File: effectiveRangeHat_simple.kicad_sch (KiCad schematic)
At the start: 11 parts, among them J1 Raspberry_Pi_2_3, P1 USB4105GFA120

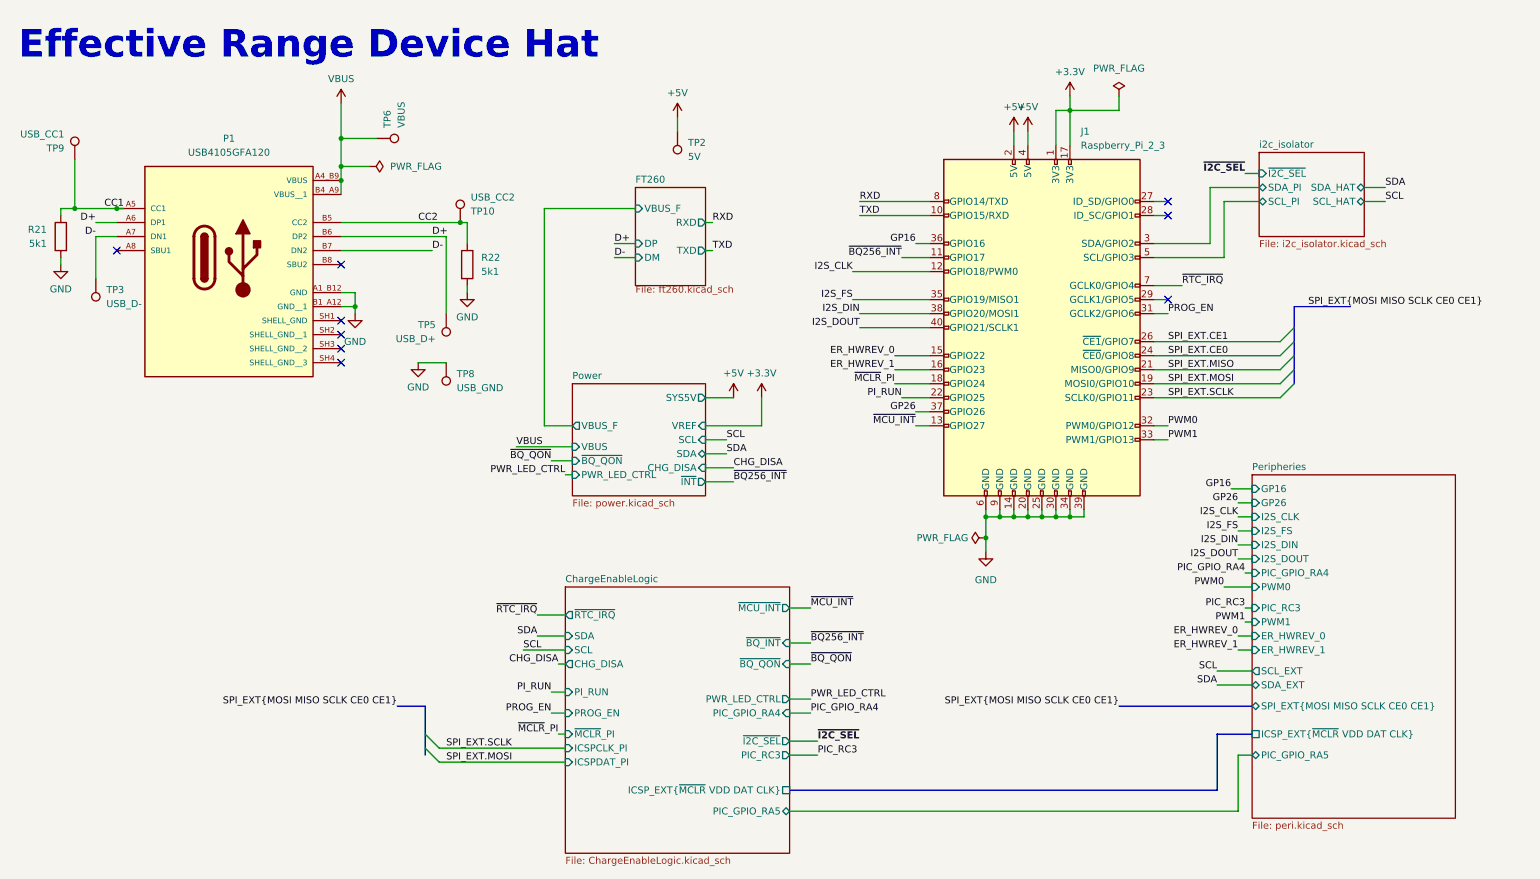
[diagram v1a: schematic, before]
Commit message: fix: modifications after driver completion
- Added missing RTC IRQ to PI
- RTC VBAT is not connected to the Main Battery trough a ~1k resistor
- Connected BQ CE through a Push-pull to Open-Drain converter to PI
- Changed Mosfets to TI PicoStar model
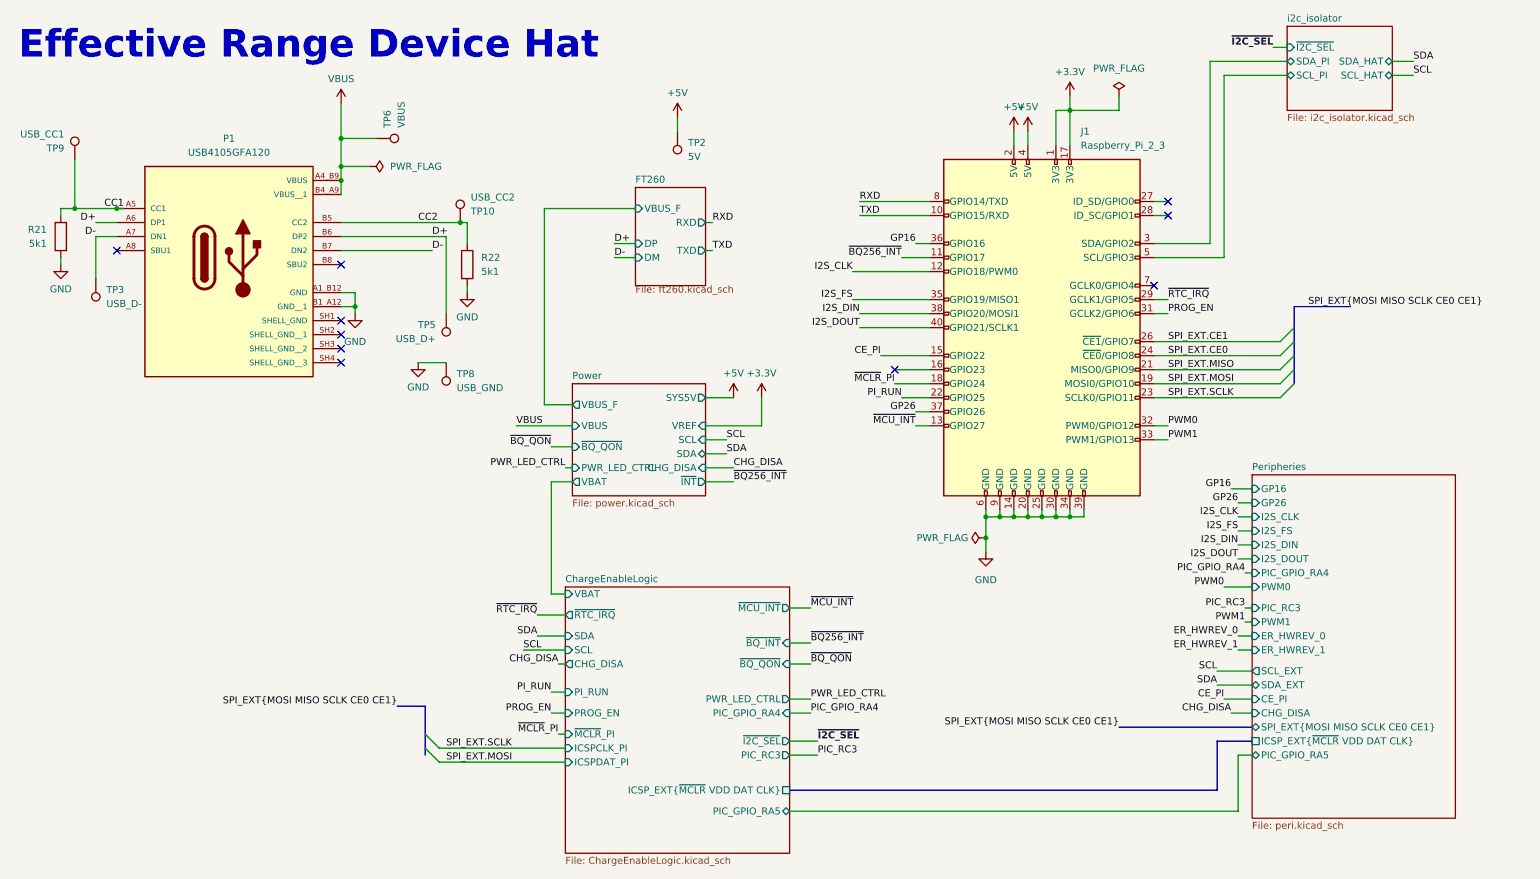
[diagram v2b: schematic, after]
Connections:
- net ER_HWREV_0: no longer J1.15 (GPIO22)
- net ER_HWREV_1: no longer J1.16 (GPIO23)
- net ~{RTC_IRQ}: now also J1.29 (GCLK1/GPIO5); no longer J1.7 (GCLK0/GPIO4)
- new net CE_PI: J1.15 (GPIO22)
- no-connect marks 9 -> 10
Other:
- sheet ChargeEnableLogic ports: added VBAT; removed none
- sheet Peripheries ports: added CE_PI, CHG_DISA; removed none
- sheet Power ports: added VBAT; removed none

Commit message: fix: erc errors
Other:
- sheet Peripheries ports: added none; removed ER_HWREV_0, ER_HWREV_1
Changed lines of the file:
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@@
 	(wire
 		(pts
-			(xy 237.49 127) (xy 240.03 127)
-		)
-		(stroke
-			(width 0)
-			(type default)
-		)
-	)
-	(wire
-		(pts
 			(xy 92.71 149.86) (xy 115.57 149.86)
 		)
@@
 	(wire
 		(pts
-			(xy 237.49 129.54) (xy 240.03 129.54)
-		)
-		(stroke
-			(width 0)
-			(type default)
-		)
-	)
-	(wire
-		(pts
 			(xy 234.95 25.4) (xy 234.95 58.42)
 		)
@@
 		)
 	)
-	(label "ER_HWREV_1"
-		(at 237.49 129.54 180)
-		(fields_autoplaced yes)
-		(effects
-			(font
-				(size 1.27 1.27)
-			)
-			(justify right bottom)
-		)
-	)
 	(label "CC1"
 		(at 35.56 49.53 180)
@@
 		)
 	)
-	(label "ER_HWREV_0"
-		(at 237.49 127 180)
-		(fields_autoplaced yes)
-		(effects
-			(font
-				(size 1.27 1.27)
-			)
-			(justify right bottom)
-		)
-	)
 	(label "~{BQ256_INT}"
 		(at 146.05 99.06 0)
@@
 			(effects
 				(font
-					(size 1.27 1.27)
-				)
-				(justify left)
-			)
-		)
-		(pin "ER_HWREV_1" input
-			(at 240.03 129.54 180)
-			(effects
-				(font
-					(size 1.27 1.27)
-				)
-				(justify left)
-			)
-		)
-		(pin "ER_HWREV_0" input
-			(at 240.03 127 180)
-			(effects
-				(font

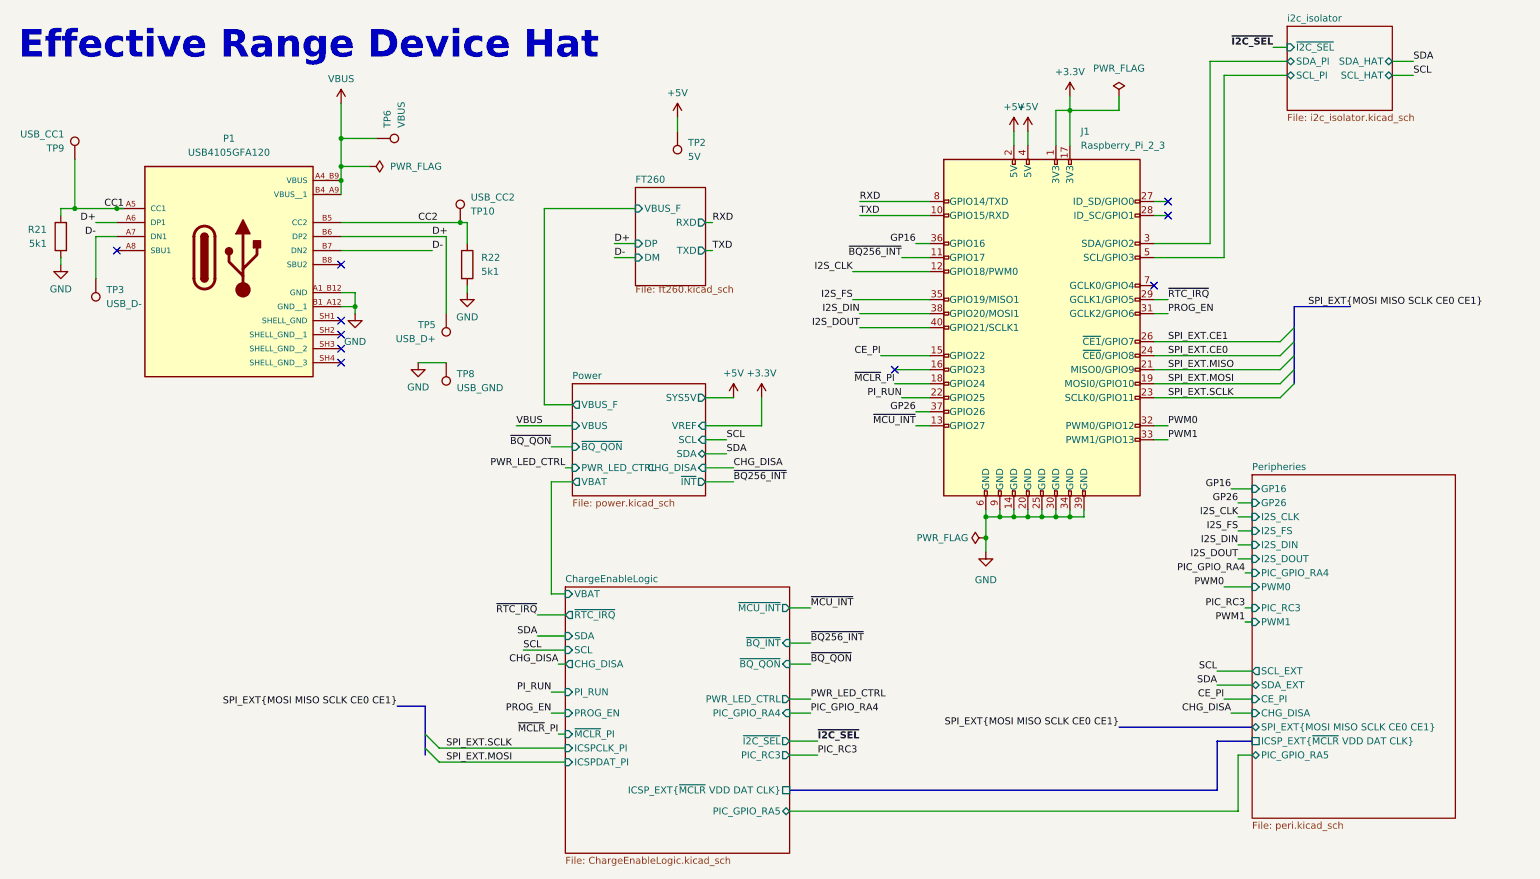
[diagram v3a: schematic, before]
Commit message: fix: pcb changes, moved i2c ext header to 2x2 pin at the edge, pinout adjustments, silkscreen fixes
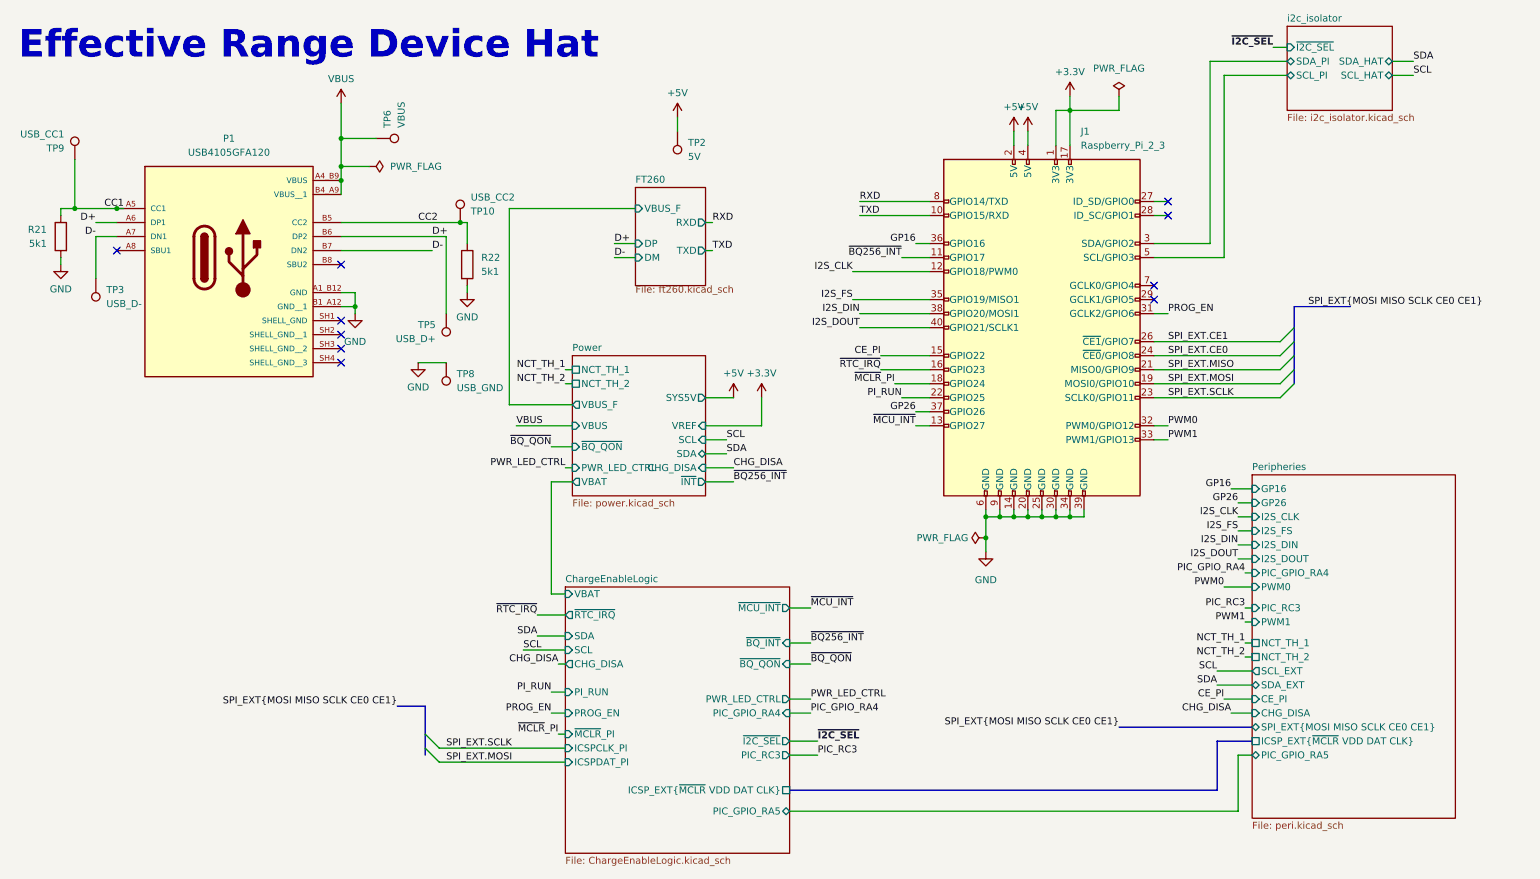
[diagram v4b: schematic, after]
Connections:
- net ~{RTC_IRQ}: now also J1.16 (GPIO23); no longer J1.29 (GCLK1/GPIO5)
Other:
- sheet Peripheries ports: added NCT_TH_1, NCT_TH_2; removed none
- sheet Power ports: added NCT_TH_1, NCT_TH_2; removed none
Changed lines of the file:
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@@
 	)
 	(no_connect
+		(at 222.25 66.04)
+	)
+	(no_connect
 		(at 74.93 77.47)
 	)
@@
 		(at 74.93 69.85)
 	)
-	(no_connect
-		(at 175.26 78.74)
-	)
 	(bus_entry
 		(at 247.65 71.12)
@@
 	(wire
 		(pts
-			(xy 111.76 85.09) (xy 111.76 49.53)
+			(xy 105.41 85.09) (xy 105.41 49.53)
 		)
 		(stroke
@@
 	(wire
 		(pts
-			(xy 111.76 85.09) (xy 116.84 85.09)
+			(xy 105.41 85.09) (xy 116.84 85.09)
 		)
 		(stroke
@@
 	(wire
 		(pts
-			(xy 222.25 66.04) (xy 224.79 66.04)
-		)
-		(stroke
-			(width 0)
-			(type default)
-		)
-	)
-	(wire
-		(pts
 			(xy 74.93 36.83) (xy 74.93 41.91)
 		)
@@
 	(wire
 		(pts
+			(xy 115.57 78.74) (xy 116.84 78.74)
+		)
+		(stroke
+			(width 0)
+			(type default)
+		)
+	)
+	(wire
+		(pts
 			(xy 222.25 55.88) (xy 232.41 55.88)
 		)
@@
 	(wire
 		(pts
-			(xy 111.76 49.53) (xy 128.27 49.53)
+			(xy 105.41 49.53) (xy 128.27 49.53)
+		)
+		(stroke
+			(width 0)
+			(type default)
+		)
+	)
+	(wire
+		(pts
+			(xy 238.76 130.81) (xy 240.03 130.81)
 		)
 		(stroke
@@
 	(wire
 		(pts
+			(xy 172.72 78.74) (xy 181.61 78.74)
+		)
+		(stroke
+			(width 0)
+			(type default)
+		)
+	)
+	(wire
+		(pts
 			(xy 114.3 132.08) (xy 115.57 132.08)
 		)
@@
 	(wire
 		(pts
-			(xy 175.26 78.74) (xy 181.61 78.74)
-		)
-		(stroke
-			(width 0)
-			(type default)
-		)
-	)
-	(wire
-		(pts
 			(xy 204.47 31.75) (xy 207.01 31.75)
 		)
@@
 	(wire
 		(pts
+			(xy 115.57 81.28) (xy 116.84 81.28)
+		)
+		(stroke
+			(width 0)
+			(type default)
+		)
+	)
+	(wire
+		(pts
 			(xy 209.55 105.41) (xy 207.01 105.41)
 		)
@@
 	(wire
 		(pts
+			(xy 238.76 128.27) (xy 240.03 128.27)
+		)
+		(stroke
+			(width 0)
+			(type default)
+		)
+	)
+	(wire
+		(pts
 			(xy 237.49 148.59) (xy 240.03 148.59)
 		)
@@
 	)
 	(label "~{RTC_IRQ}"
-		(at 224.79 66.04 0)
+		(at 172.72 78.74 180)
 		(fields_autoplaced yes)
 		(effects
@@
 				(size 1.27 1.27)
 			)
-			(justify left bottom)
+			(justify right bottom)
 		)
 	)
@@
 		)
 	)
+	(label "NCT_TH_1"
+		(at 238.76 128.27 180)
+		(fields_autoplaced yes)
+		(effects
+			(font
+				(size 1.27 1.27)
+			)
+			(justify right bottom)
+		)
+	)
 	(label "D-"
 		(at 91.44 57.15 0)
@@
 		)
 	)
+	(label "NCT_TH_1"
+		(at 115.57 78.74 180)
+		(fields_autoplaced yes)
+		(effects
+			(font
+				(size 1.27 1.27)
+			)
+			(justify right bottom)
+		)
+	)
 	(label "SPI_EXT.SCLK"
 		(at 93.98 147.32 0)
@@
 		)
 	)
+	(label "NCT_TH_2"
+		(at 115.57 81.28 180)
+		(fields_autoplaced yes)
+		(effects
+			(font
+				(size 1.27 1.27)
+			)
+			(justify right bottom)
+		)
+	)
 	(label "RXD"
 		(at 168.91 48.26 0)
@@
 		)
 	)
+	(label "NCT_TH_2"
+		(at 238.76 130.81 180)
+		(fields_autoplaced yes)
+		(effects
+			(font
+				(size 1.27 1.27)
+			)
+			(justify right bottom)
+		)
+	)
 	(label "~{BQ_QON}"
 		(at 160.02 132.08 0)
@@
 			)
 		)
+		(pin "NCT_TH_2" passive
+			(at 240.03 130.81 180)
+			(effects
+				(font
+					(size 1.27 1.27)
+				)
+				(justify left)
+			)
+		)
+		(pin "NCT_TH_1" passive
+			(at 240.03 128.27 180)
+			(effects
+				(font
+					(size 1.27 1.27)
+				)
+				(justify left)
+			)
+		)
 		(instances
 			(project "effectiveRangeHat_simple"
@@
 	)
 	(sheet
-		(at 116.84 81.28)
-		(size 24.13 20.32)
+		(at 116.84 76.2)
+		(size 24.13 25.4)
 		(fields_autoplaced yes)
 		(stroke
@@
 		)
 		(property "Sheetname" "Power"
-			(at 116.84 80.5684 0)
+			(at 116.84 75.4884 0)
 			(effects
 				(font
@@
 			(effects
 				(font
+					(size 1.27 1.27)
+				)
+				(justify left)
+			)
+		)
+		(pin "NCT_TH_1" passive
+			(at 116.84 78.74 180)
+			(effects
+				(font
+					(size 1.27 1.27)
+				)
+				(justify left)
+			)
+		)
+		(pin "NCT_TH_2" passive
+			(at 116.84 81.28 180)
+			(effects
+				(font
